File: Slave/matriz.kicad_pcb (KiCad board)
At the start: 2 copper layers, 32 parts, among them J1 Conn_01x05, J2 Conn_01x05, J3 Conn_01x08, J4 Conn_01x08, U1 MAX7219

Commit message: Pistas todas de 1mm, limite y unidades mecanicas
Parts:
- added REF**: 1pin, Connectors:1pin, F.Cu at (113.0, 134.0)
- added REF**: 1pin, Connectors:1pin, F.Cu at (190.0, 73.0)
- added REF**: 1pin, Connectors:1pin, F.Cu at (189.0, 134.0)
- added REF**: 1pin, Connectors:1pin, F.Cu at (113.0, 73.0)
- CP1: footprint Capacitors_SMD:CP_Elec_6.3x5.7 -> Capacitors_THT:CP_Radial_Tantal_D7.0mm_P5.00mm
- J1, J2: footprint Pin_Headers:Pin_Header_Angled_1x05_Pitch2.54mm -> Pin_Headers:Pin_Header_Straight_1x05_Pitch2.54mm
- J3, J4: footprint Pin_Headers:Pin_Header_Angled_1x08_Pitch2.54mm -> Pin_Headers:Pin_Header_Straight_1x08_Pitch2.54mm
- moved J2 28.3 mm to (168.0, 73.0)
- moved w12.1 19.5 mm to (131.0, 86.0)
- moved J1 12.1 mm to (113.0, 80.0)
- moved w12.2 11.4 mm to (123.0, 83.0)
- moved w9.2 9.49 mm to (157.0, 133.0)
- moved w1.2 8.97 mm to (179.0, 84.0)
- moved w1.1 8.06 mm to (172.0, 85.0)
- moved w11.1 8.06 mm to (166.0, 86.0)
- moved w5.2 8.06 mm to (167.0, 104.0)
- moved CP1 7.43 mm to (129.0, 79.0)
- moved J3 5.43 mm to (180.0, 88.0)
- moved w11.2 5.39 mm to (177.0, 100.0)
- moved w3.1 5.10 mm to (162.0, 101.0)
- moved w4.1 5.10 mm to (167.0, 94.0)
- moved w4.2 5.10 mm to (173.0, 100.0)
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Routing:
- net /GND: track 238.7 -> 184.2 mm
- net /CLK: track 226.4 -> 189.6 mm
- net /DOUT: track 48.8 -> 19.0 mm
- net /LD: track 159.9 -> 133.3 mm
- net /DIN: track 41.6 -> 21.2 mm
- net /V+: track 123.2 -> 109.7 mm
- net /C5: track 56.0 -> 43.5 mm
- net /F3: track 20.3 -> 9.18 mm
- net /F0: track 29.6 -> 19.8 mm
- net /F7: track 28.3 -> 20.5 mm
- net /F5: track 32.7 -> 27.1 mm
- net /F1: track 29.5 -> 23.9 mm
- net /F6: track 53.8 -> 48.3 mm
- net /C0: track 88.1 -> 92.5 mm
- net /F4: track 23.9 -> 20.0 mm
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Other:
- board outline added: 88 x 72 mm
- net class Default: trace_width 0.6 -> 1

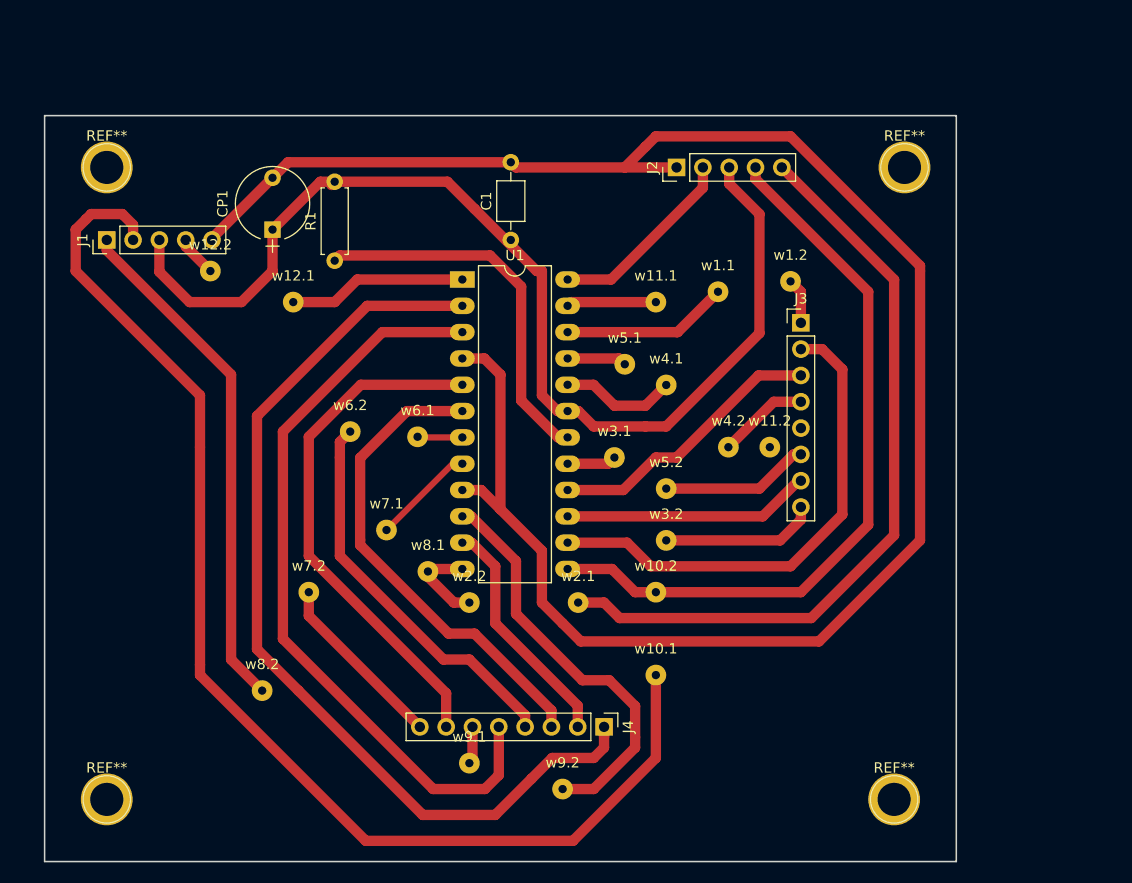
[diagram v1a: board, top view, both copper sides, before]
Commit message: Pongo las pistas en para que sea lo de atras (en verde) y minimiso espacio
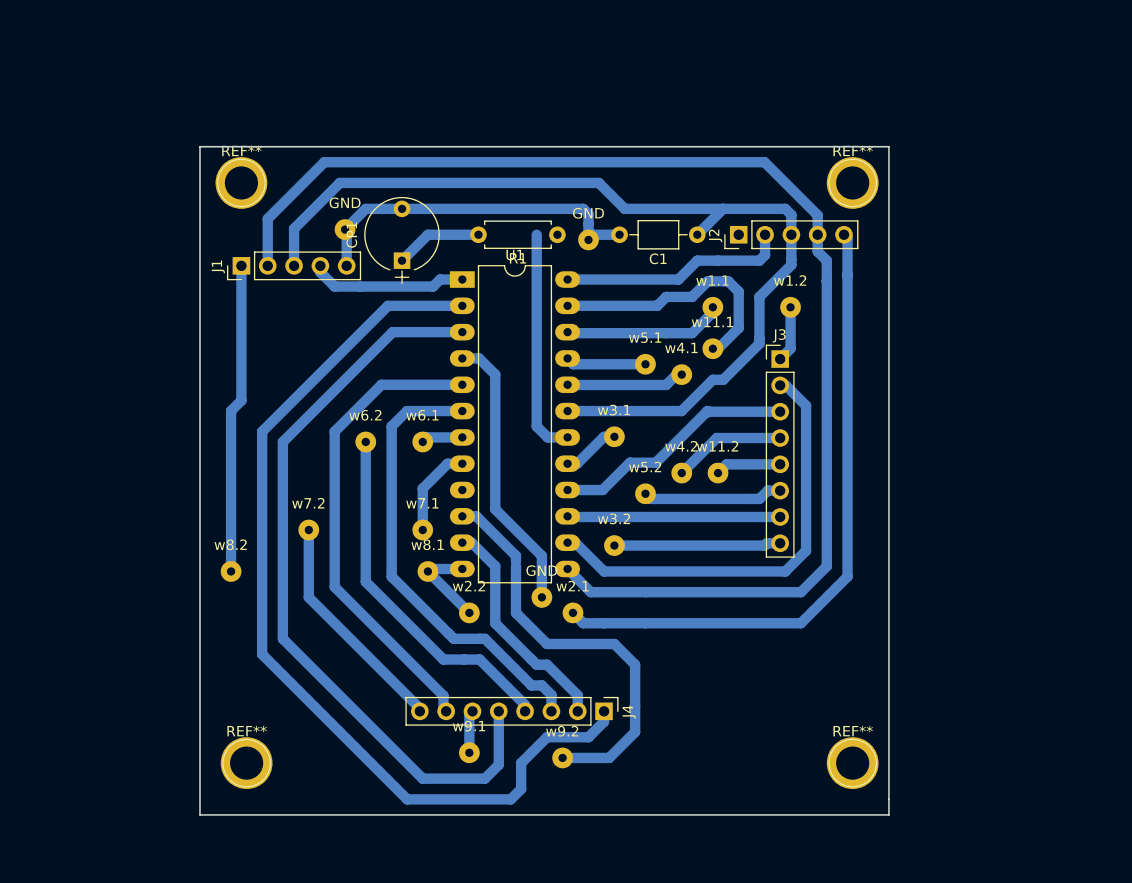
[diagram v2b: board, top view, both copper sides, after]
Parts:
- removed w10.1, w10.2, w12.1, w12.2: , Wire_Pads:SolderWirePad_single_0-8mmDrill
- added GND: , Wire_Pads:SolderWirePad_single_0-8mmDrill, F.Cu at (136.0, 79.0)
- added GND: , Wire_Pads:SolderWirePad_single_0-8mmDrill, F.Cu at (155.0, 114.5)
- added GND: , Wire_Pads:SolderWirePad_single_0-8mmDrill, F.Cu at (159.5, 80.0)
- moved R1 21.6 mm to (156.5, 79.5), turned to 180 degrees
- moved C1 18.0 mm to (170.0, 79.5), turned to 180 degrees
- moved REF** 13.9 mm to (126.5, 130.5)
- moved J1 13.2 mm to (126.0, 82.5)
- moved REF** 13.1 mm to (126.0, 74.5)
- moved CP1 12.9 mm to (141.5, 82.0)
- moved w8.2 11.9 mm to (125.0, 112.0)
- moved J2 8.85 mm to (174.0, 79.5)
- moved w11.1 7.11 mm to (171.5, 90.5)
- moved w7.2 6.00 mm to (132.5, 108.0)
- moved w11.2 5.59 mm to (172.0, 102.5)
- moved REF** 5.32 mm to (185.0, 130.5)
- moved REF** 5.22 mm to (185.0, 74.5)
- moved w4.2 5.15 mm to (168.5, 102.5)
- moved w3.2 5.02 mm to (162.0, 109.5)
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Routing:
- net /GND: track 184.2 -> 61.5 mm
- net /CLK: track 189.6 -> 123.4 mm
- net /LD: track 133.3 -> 101.2 mm
- net /F3: track 9.18 -> 30.6 mm
- net Net-(R1-Pad1): track 36.8 -> 23.3 mm
- net /V+: track 109.7 -> 101.6 mm
- net /F6: track 48.3 -> 42.3 mm
- net /DIN: track 21.2 -> 15.2 mm
- net /C6: track 50.4 -> 45.6 mm
- net /C7: track 27.4 -> 31.7 mm
- net /C3: track 42.5 -> 38.5 mm
- net /F1: track 23.9 -> 20.5 mm
- net /C2: track 46.8 -> 43.7 mm
- net /DOUT: track 19.0 -> 22.0 mm
- net /F5: track 27.1 -> 24.8 mm
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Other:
- board size 88 x 72 mm -> 66.5 x 64.5 mm

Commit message: Avances entre todos
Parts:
- removed w2.1, w2.2, w8.1, w8.2: , Wire_Pads:SolderWirePad_single_0-8mmDrill
- moved w9.1 34.8 mm to (137.0, 96.5)
- moved J4 34.2 mm to (131.0, 109.0), turned to 180 degrees
- moved w9.2 30.9 mm to (137.0, 106.5)
- moved GND 25.5 mm to (144.0, 91.5)
- moved w7.2 18.6 mm to (141.0, 91.5)
- moved REF** 12.0 mm to (126.0, 118.5)
- moved REF** 12.0 mm to (185.0, 118.5)
- moved w7.1 6.50 mm to (141.0, 102.0)
- moved w1.1 4.92 mm to (167.0, 88.5)
- moved w6.2 3.54 mm to (134.5, 99.0)
- moved J2 3.04 mm to (173.5, 82.5)
- moved w4.1 2.24 mm to (166.5, 94.0)
- moved w1.2 2.06 mm to (179.5, 88.5)
- moved w11.1 2.06 mm to (169.5, 91.0)
- moved w11.2 2.00 mm to (170.0, 102.5)
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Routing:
- net /C0: track 90.2 -> 45.5 mm
- net /C4: track 72.9 -> 30.5 mm
- net /C3: track 38.5 -> 9.12 mm
- net /C6: track 45.6 -> 16.4 mm
- net /C5: track 44.0 -> 16.0 mm
- net /C2: track 43.7 -> 19.4 mm
- net /LD: track 101.2 -> 121.2 mm
- net /C7: track 31.7 -> 16.6 mm
- net /F7: track 20.9 -> 13.3 mm
- net /F3: track 30.6 -> 24.5 mm
- net /V+: track 101.6 -> 105.3 mm
- net /C1: track 22.0 -> 18.4 mm
- net /CLK: track 123.4 -> 121.2 mm
- net /GND: track 61.5 -> 63.4 mm
- net Net-(R1-Pad1): track 23.3 -> 21.5 mm
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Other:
- board size 66.5 x 64.5 mm -> 66.5 x 51.5 mm

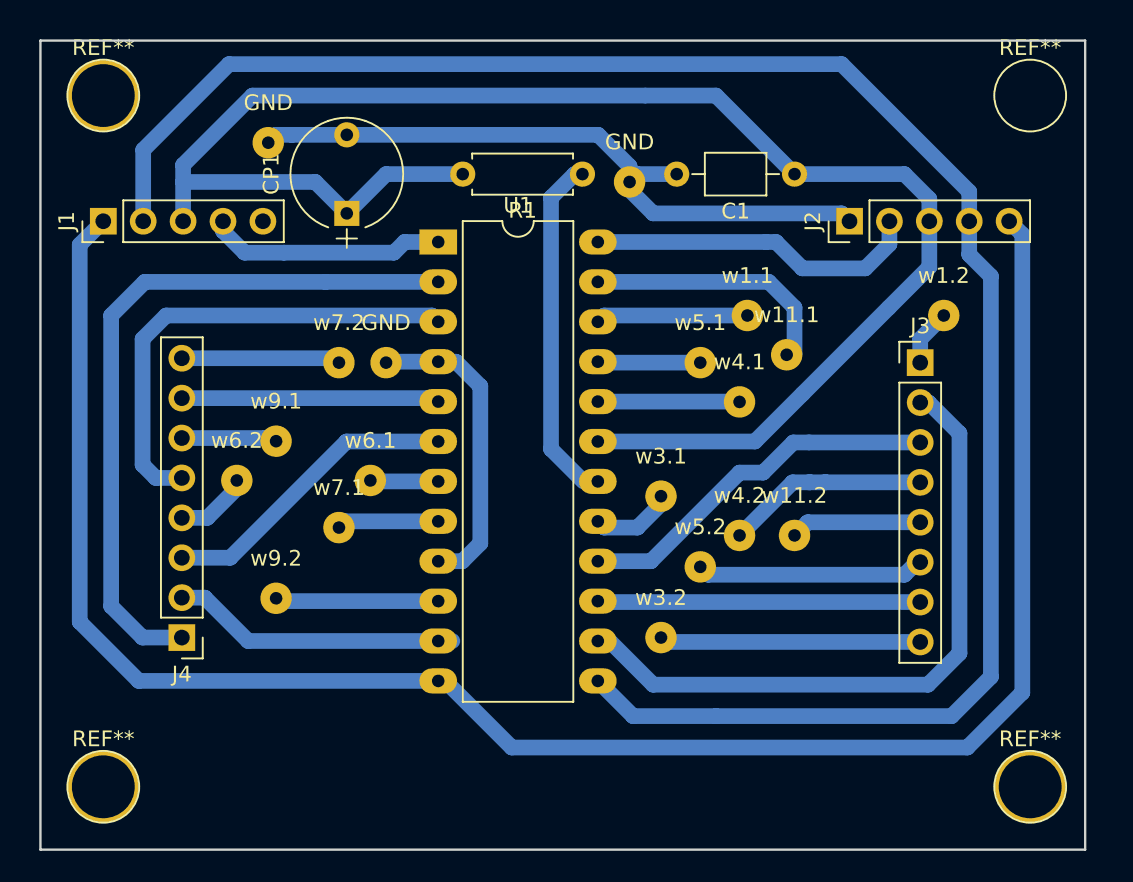
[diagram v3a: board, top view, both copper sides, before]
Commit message: Generacion de pdf final con limites y otras cosas
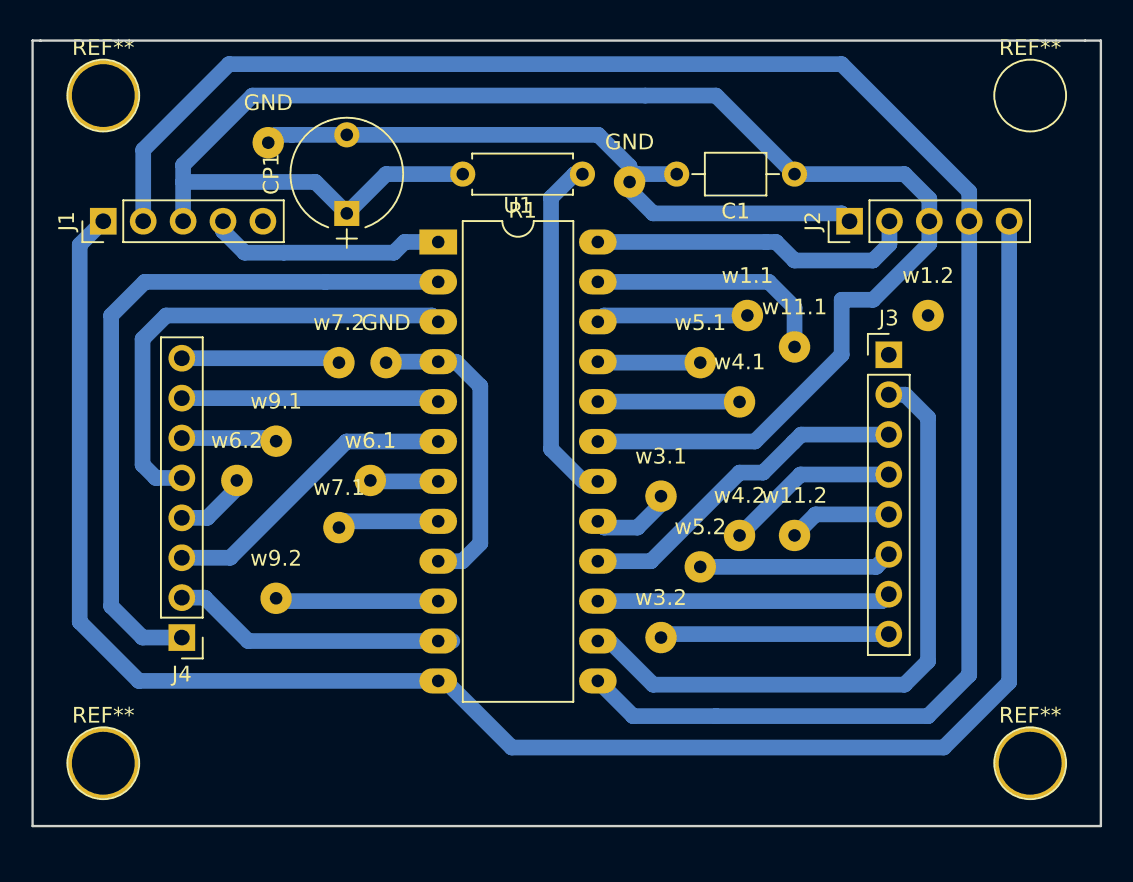
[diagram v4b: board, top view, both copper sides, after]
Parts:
- moved J3 2.06 mm to (176.0, 91.0)
- moved REF** 1.50 mm to (126.0, 117.0)
- moved REF** 1.50 mm to (185.0, 117.0)
- moved w1.2 1.00 mm to (178.5, 88.5)
- moved w11.1 0.71 mm to (170.0, 90.5)
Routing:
- net /F7: track 13.3 -> 9.69 mm
- net /F2: track 21.1 -> 18.9 mm
- net /F4: track 22.2 -> 20.1 mm
- net /CLK: track 121.2 -> 119.2 mm
- net /F5: track 24.6 -> 22.7 mm
- net /F3: track 24.5 -> 22.8 mm
- net /F1: track 20.5 -> 18.8 mm
- net /F0: track 21.9 -> 20.3 mm
- net /LD: track 121.2 -> 119.7 mm
- net /V+: track 105.3 -> 106.5 mm
- net /F6: track 42.3 -> 41.4 mm
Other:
- board size 66.5 x 51.5 mm -> 68 x 50 mm

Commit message: Ultimos cambios
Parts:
- added REF**: SolderWirePad_single_0-8mmDrill, Wire_Pads:SolderWirePad_single_0-8mmDrill, F.Cu at (138.0, 82.0)
- U1: footprint Housings_DIP:DIP-24_W10.16mm_LongPads -> Housings_DIP:DIP-24_W7.62mm_LongPads
- moved U1 2.69 mm to (150.0, 84.0)
- moved J1 1.12 mm to (125.0, 83.0)
- moved w1.2 0.71 mm to (178.0, 88.0)
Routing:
- net /GND: track 63.4 -> 70.1 mm
- net /F7: track 9.69 -> 13.5 mm
- net /DIN: track 15.2 -> 19.0 mm
- net /C7: track 16.6 -> 19.8 mm
- net /C5: track 16.0 -> 19.0 mm
- net /C6: track 16.4 -> 19.2 mm
- net /C3: track 9.12 -> 11.9 mm
- net /C2: track 19.4 -> 22.0 mm
- net /C0: track 45.5 -> 48.1 mm
- net /C4: track 30.5 -> 32.9 mm
- net /V+: track 106.5 -> 108.5 mm
- net /C1: track 18.4 -> 20.2 mm
- net /CLK: track 119.2 -> 120.4 mm
- net Net-(R1-Pad1): track 21.5 -> 22.5 mm
- net /LD: track 119.7 -> 118.8 mm

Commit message: Pads adecuados
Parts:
- moved CP1 2.01 mm to (143.5, 81.9)
- moved GND 0.94 mm to (137.2, 76.8)
- moved REF** 0.87 mm to (184.2, 74.3)
- moved REF** 0.86 mm to (184.2, 116.8)
- moved REF** 0.70 mm to (138.4, 82.5)
- moved J1 0.46 mm to (125.1, 82.5)
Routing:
- net /DIN: track 19.0 -> 20.1 mm
- net /C0: track 48.1 -> 49.3 mm
- net /LD: track 118.8 -> 119.8 mm
- net /GND: track 70.1 -> 69.3 mm
- net /C4: track 32.9 -> 33.6 mm
- net /F6: track 41.4 -> 42.1 mm
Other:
- board size 68 x 50 mm -> 66 x 51 mm

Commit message: fix
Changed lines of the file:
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@@
   (general
     (links 53)
-    (no_connects 11)
+    (no_connects 10)
     (area 121.79 69.924999 198.85 126.700001)
     (thickness 1.6)
     (drawings 6)
-    (tracks 162)
+    (tracks 163)
     (zones 0)
     (modules 32)
@@
     (mod_text_size 1 1)
     (mod_text_width 0.15)
-    (pad_size 2 2)
+    (pad_size 2.5 1.5)
     (pad_drill 0.7)
     (pad_to_mask_clearance 0.2)
@@
       (effects (font (size 1 1) (thickness 0.15)))
     )
-    (pad 1 thru_hole rect (at 0 0 90) (size 2.5 1.7) (drill 1) (layers *.Cu *.Mask)
+    (pad 1 thru_hole rect (at 0 0 90) (size 2.5 1.7) (drill 0.7) (layers *.Cu *.Mask)
       (net 3 /LD))
     (pad 2 thru_hole oval (at 0 2.54 90) (size 2.5 1.7) (drill 0.7) (layers *.Cu *.Mask)
@@
     (pad 19 thru_hole oval (at 7.62 12.7) (size 2.5 1.5) (drill 0.7) (layers *.Cu *.Mask)
       (net 1 /V+))
-    (pad 8 thru_hole oval (at 0 17.78) (size 2.4 1.6) (drill 0.8) (layers *.Cu *.Mask)
+    (pad 8 thru_hole oval (at 0 17.78) (size 2.4 1.6) (drill 0.7) (layers *.Cu *.Mask)
       (net 22 /C7))
     (pad 20 thru_hole oval (at 7.62 10.16) (size 2.5 1.5) (drill 0.7) (layers *.Cu *.Mask)
@@
     (pad 23 thru_hole oval (at 7.62 2.54) (size 2.5 1.5) (drill 0.7) (layers *.Cu *.Mask)
       (net 11 /F3))
-    (pad 12 thru_hole oval (at 0 27.94) (size 2.5 1.5) (drill 0.8) (layers *.Cu *.Mask)
+    (pad 12 thru_hole oval (at 0 27.94) (size 2.5 1.5) (drill 0.7) (layers *.Cu *.Mask)
       (net 3 /LD))
     (pad 24 thru_hole oval (at 7.62 0) (size 2.5 1.5) (drill 0.7) (layers *.Cu *.Mask)
@@
   (segment (start 177 79.5) (end 178.58 81.08) (width 1) (layer B.Cu) (net 1))
   (segment (start 178.58 81.08) (end 178.58 82.5) (width 1) (layer B.Cu) (net 1))
+  (segment (start 143.51 76.915) (end 137.24 76.915) (width 1) (layer B.Cu) (net 2))
+  (segment (start 137.24 76.915) (end 137.16 76.835) (width 1) (layer B.Cu) (net 2))
+  (segment (start 143.595 77) (end 157.5 77) (width 1) (layer B.Cu) (net 2))
+  (segment (start 157.5 77) (end 159.5 79) (width 1) (layer B.Cu) (net 2))
+  (segment (start 143.595 77) (end 143.51 76.915) (width 1) (layer B.Cu) (net 2))
   (segment (start 138.43 82.55) (end 135.255 82.55) (width 1) (layer B.Cu) (net 2))
   (segment (start 150 91.62) (end 151.62 91.62) (width 1) (layer B.Cu) (net 2))
@@
   (segment (start 173 82) (end 173.5 82.5) (width 1) (layer B.Cu) (net 2))
   (segment (start 159.5 80) (end 159.5 79) (width 1) (layer B.Cu) (net 2))
-  (segment (start 157.5 77) (end 141.5 77) (width 1) (layer B.Cu) (net 2))
-  (segment (start 159.5 79) (end 157.5 77) (width 1) (layer B.Cu) (net 2))
   (segment (start 144.06 91.44) (end 144 91.5) (width 1) (layer B.Cu) (net 2))
-  (segment (start 137 77) (end 138 77) (width 1) (layer B.Cu) (net 2))
-  (segment (start 138 77) (end 141.5 77) (width 1) (layer B.Cu) (net 2))
   (segment (start 162.5 79.5) (end 160 79.5) (width 1) (layer B.Cu) (net 2))
   (segment (start 160 79.5) (end 159.5 80) (width 1) (layer B.Cu) (net 2))

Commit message: esta comiendo una empanada
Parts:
- removed the GND at (137.2, 76.8)
- removed the GND at (159.5, 80.0)
- moved w6.1 10.5 mm to (135.0, 105.8)
- moved w7.1 2.24 mm to (141.0, 104.2)
- moved w11.1 1.96 mm to (170.0, 92.5)
- moved w1.2 1.21 mm to (178.8, 88.9)
- moved REF** 1.08 mm to (139.2, 81.8)
- moved w9.2 1.01 mm to (138.0, 106.8)
- moved w9.1 0.93 mm to (137.9, 96.6)
- moved w11.2 0.92 mm to (170.2, 101.6)
- moved J1 0.85 mm to (125.5, 81.8)
- moved w1.1 0.70 mm to (166.8, 89.2)
- moved w6.2 0.60 mm to (135.0, 99.4)
- moved J3 0.52 mm to (176.3, 91.4)
- moved w4.2 0.41 mm to (166.6, 102.1)
- moved CP1 0.38 mm to (143.5, 81.5)
- moved J4 0.35 mm to (130.9, 109.3)
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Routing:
- net /C3: track 11.9 -> 23.8 mm
- net /GND: track 69.2 -> 59.8 mm
- net /V+: track 108.1 -> 104.8 mm
- net /DIN: track 20.1 -> 18.7 mm
- net /CLK: track 120.4 -> 119.0 mm
- net /F3: track 22.8 -> 23.9 mm
- net /LD: track 119.8 -> 120.8 mm
- net /F7: track 13.5 -> 12.8 mm
- net /C2: track 22.0 -> 22.7 mm
